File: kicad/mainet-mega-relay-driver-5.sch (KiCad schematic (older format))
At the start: 8 parts, among them J34 Screw_Terminal_01x03, K5 SANYOU_SRD_Form_C, Q5 2N3904, U6 4N37

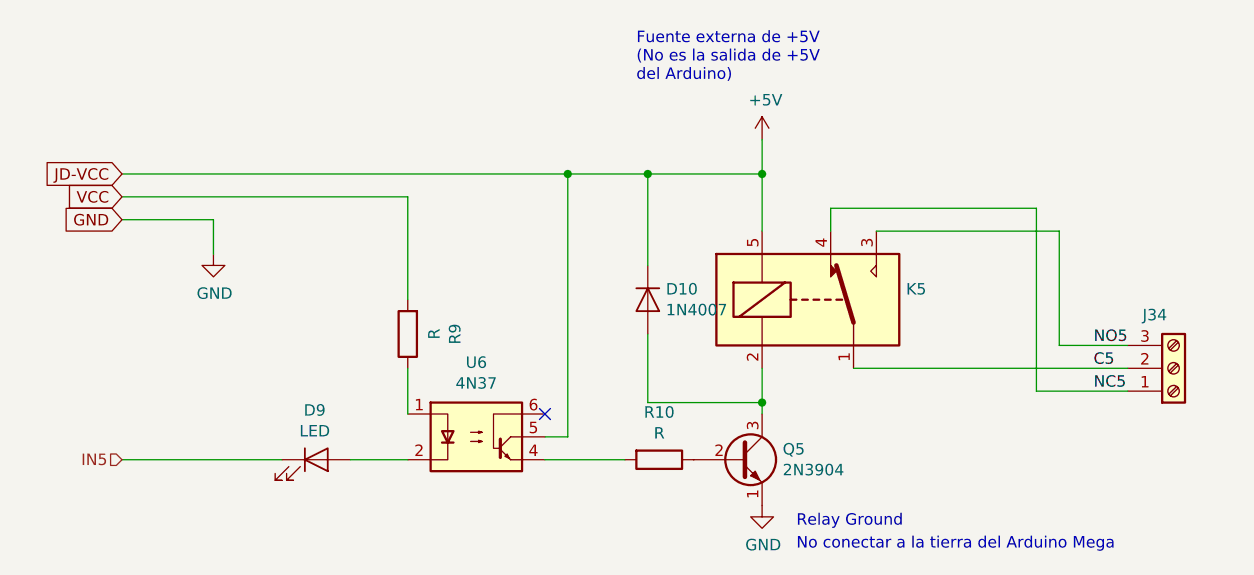
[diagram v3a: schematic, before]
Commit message: KICAD: Actualización de esquematicos del módulo de 8 relés de control
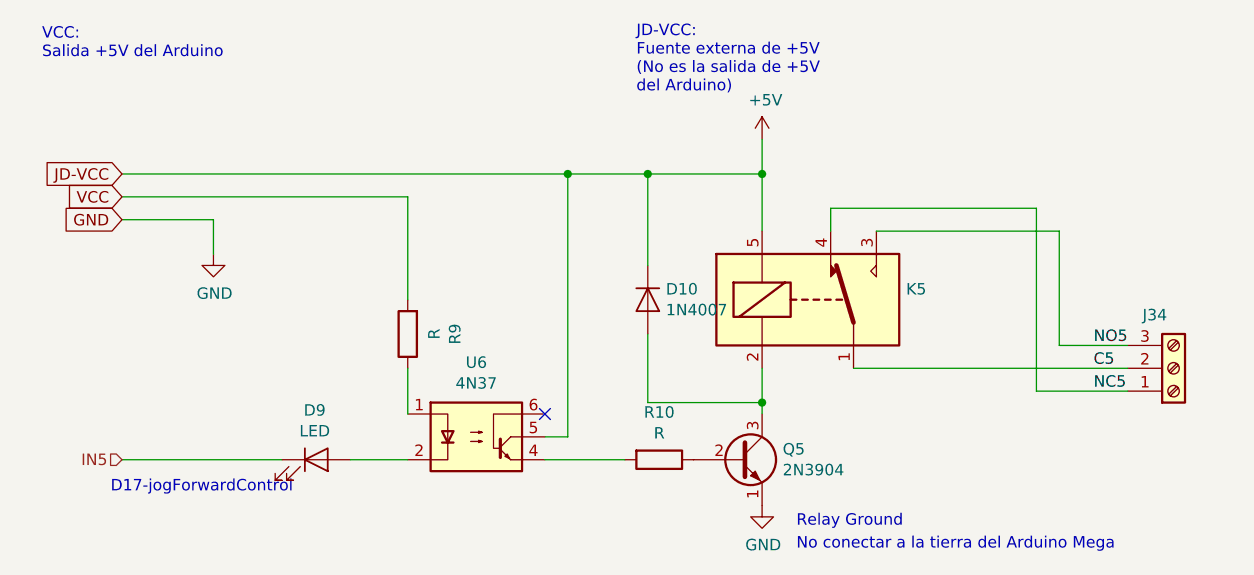
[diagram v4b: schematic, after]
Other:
- note added: "D17-jogForwardControl"
- note added: "JD-VCC:\nFuente externa de +5V\n(No es la salida de +5V \ndel Arduino)"
- note added: "VCC:\nSalida +5V del Arduino"
- note removed: "Fuente externa de +5V\n(No es la salida de +5V \ndel Arduino)"
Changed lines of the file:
@@
 EESchema Schematic File Version 4
 LIBS:mainet-mega-cache
-LIBS:mainet-mega-5V-to-mp-10v-cache
 EELAYER 30 0
 EELAYER END
 $Descr A4 11693 8268
 encoding utf-8
-Sheet 12 21
-Title ""
-Date ""
+Sheet 11 21
+Title "Relay driver 6"
+Date "2021-02-02"
 Rev ""
 Comp ""
@@
 	1    0    0    -1
 $EndComp
-Text Notes 5950 2450 0    50   ~ 0
-Fuente externa de +5V\n(No es la salida de +5V \ndel Arduino)
 Text Notes 6650 4400 0    50   ~ 0
 Relay Ground\n
@@
 Text GLabel 3700 2950 0    50   Input ~ 0
 VCC
+Text Notes 5950 2500 0    50   ~ 0
+JD-VCC:\nFuente externa de +5V\n(No es la salida de +5V \ndel Arduino)
+Text Notes 3350 2350 0    50   ~ 0
+VCC:\nSalida +5V del Arduino
+Text Notes 3650 4250 0    50   ~ 0
+D17-jogForwardControl
 $EndSCHEMATC
